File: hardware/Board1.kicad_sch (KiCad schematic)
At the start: 40 parts, among them IC1 AH1912-W-7, IC2 AH1912-W-7, J2 USB_C_Receptacle_USB2.0, J3 Conn_ST_STDC14, J4 Conn_01x02_Pin, J5 Conn_01x02_Pin, SW1 SW_Push, SW2 SW_Push, U1 STM32F042G6U6TR, U2 TS2940CW33_RPG, U3 STM32F072RBTx, U4 TJA1051T-3, Y1 8M

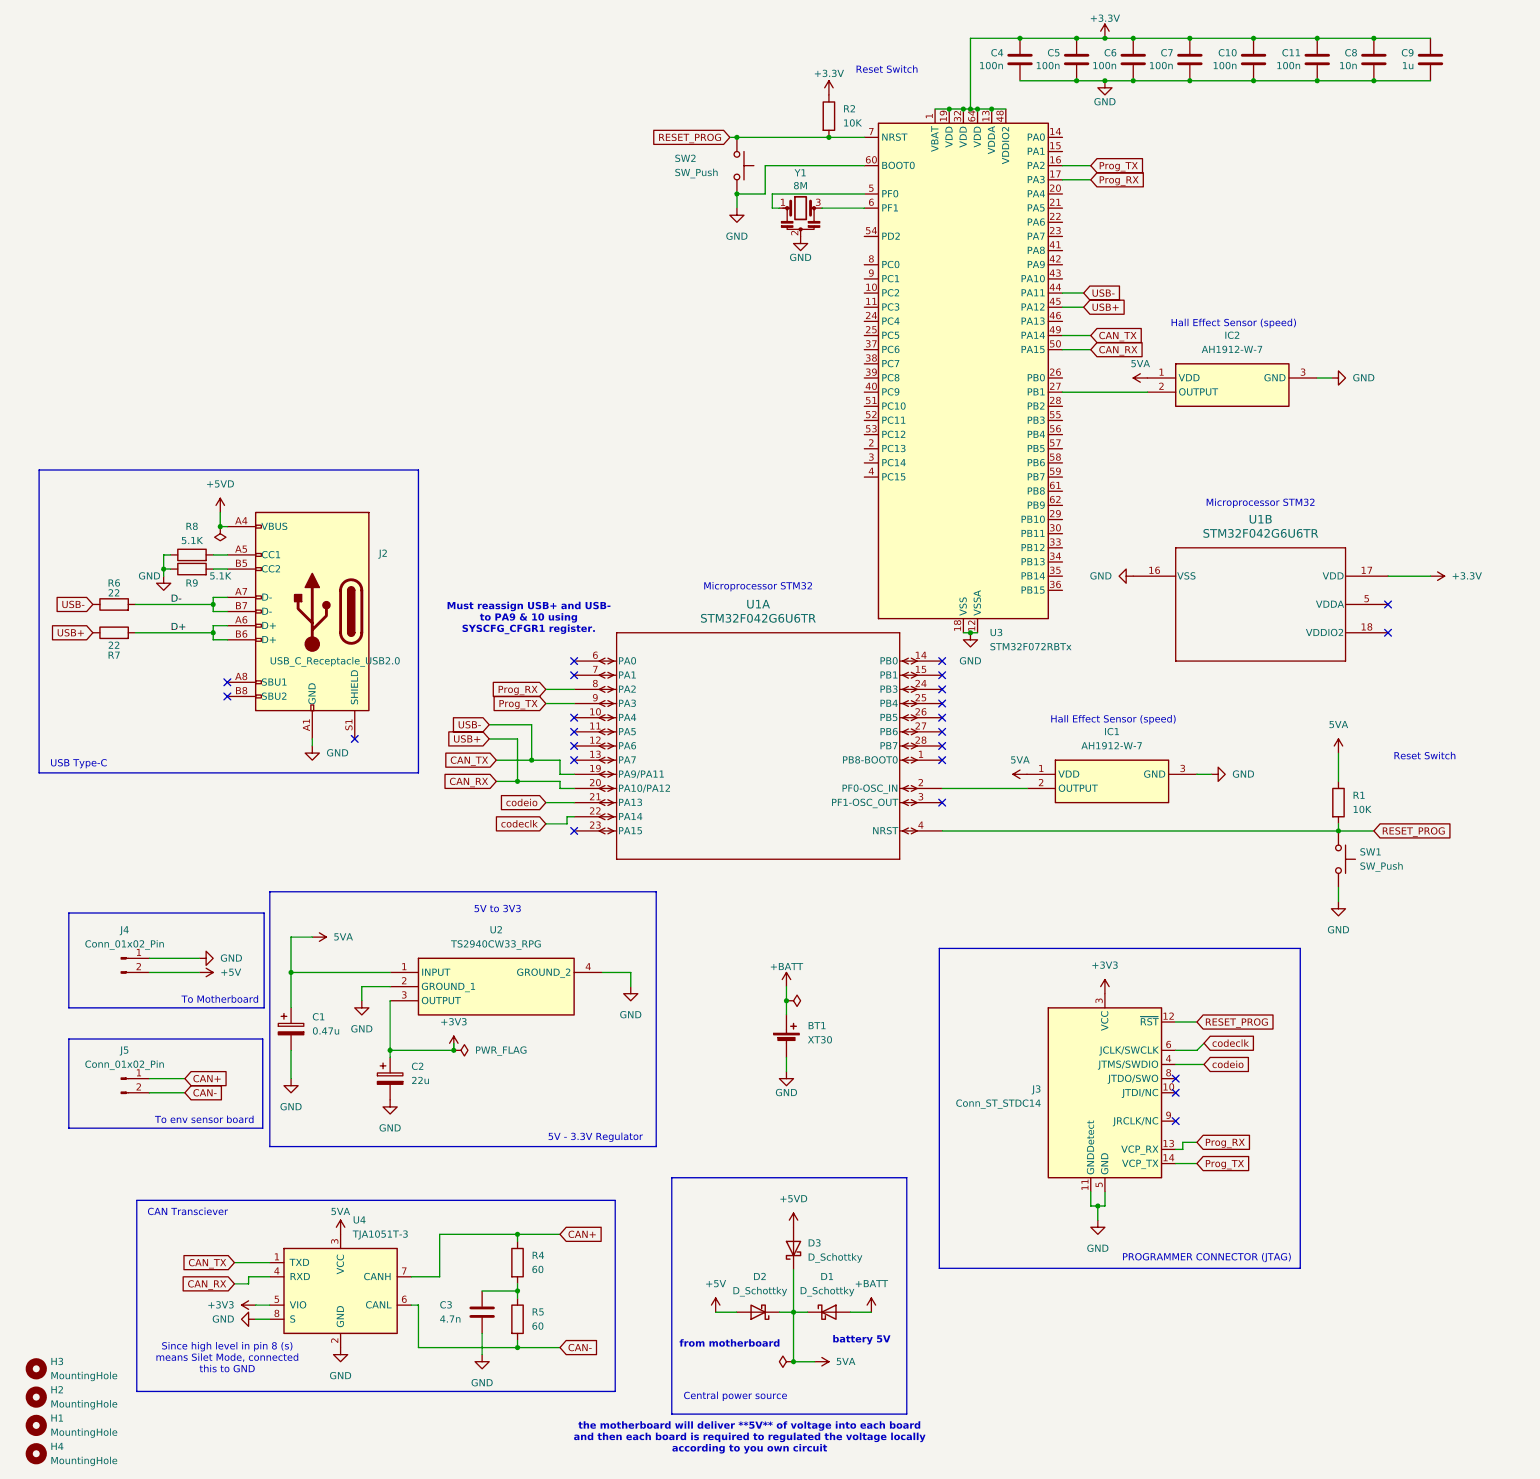
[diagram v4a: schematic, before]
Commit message: final revision of the speed and cadence board
Finished re routing the PCB and also did BOM and production needed for JLC PCB
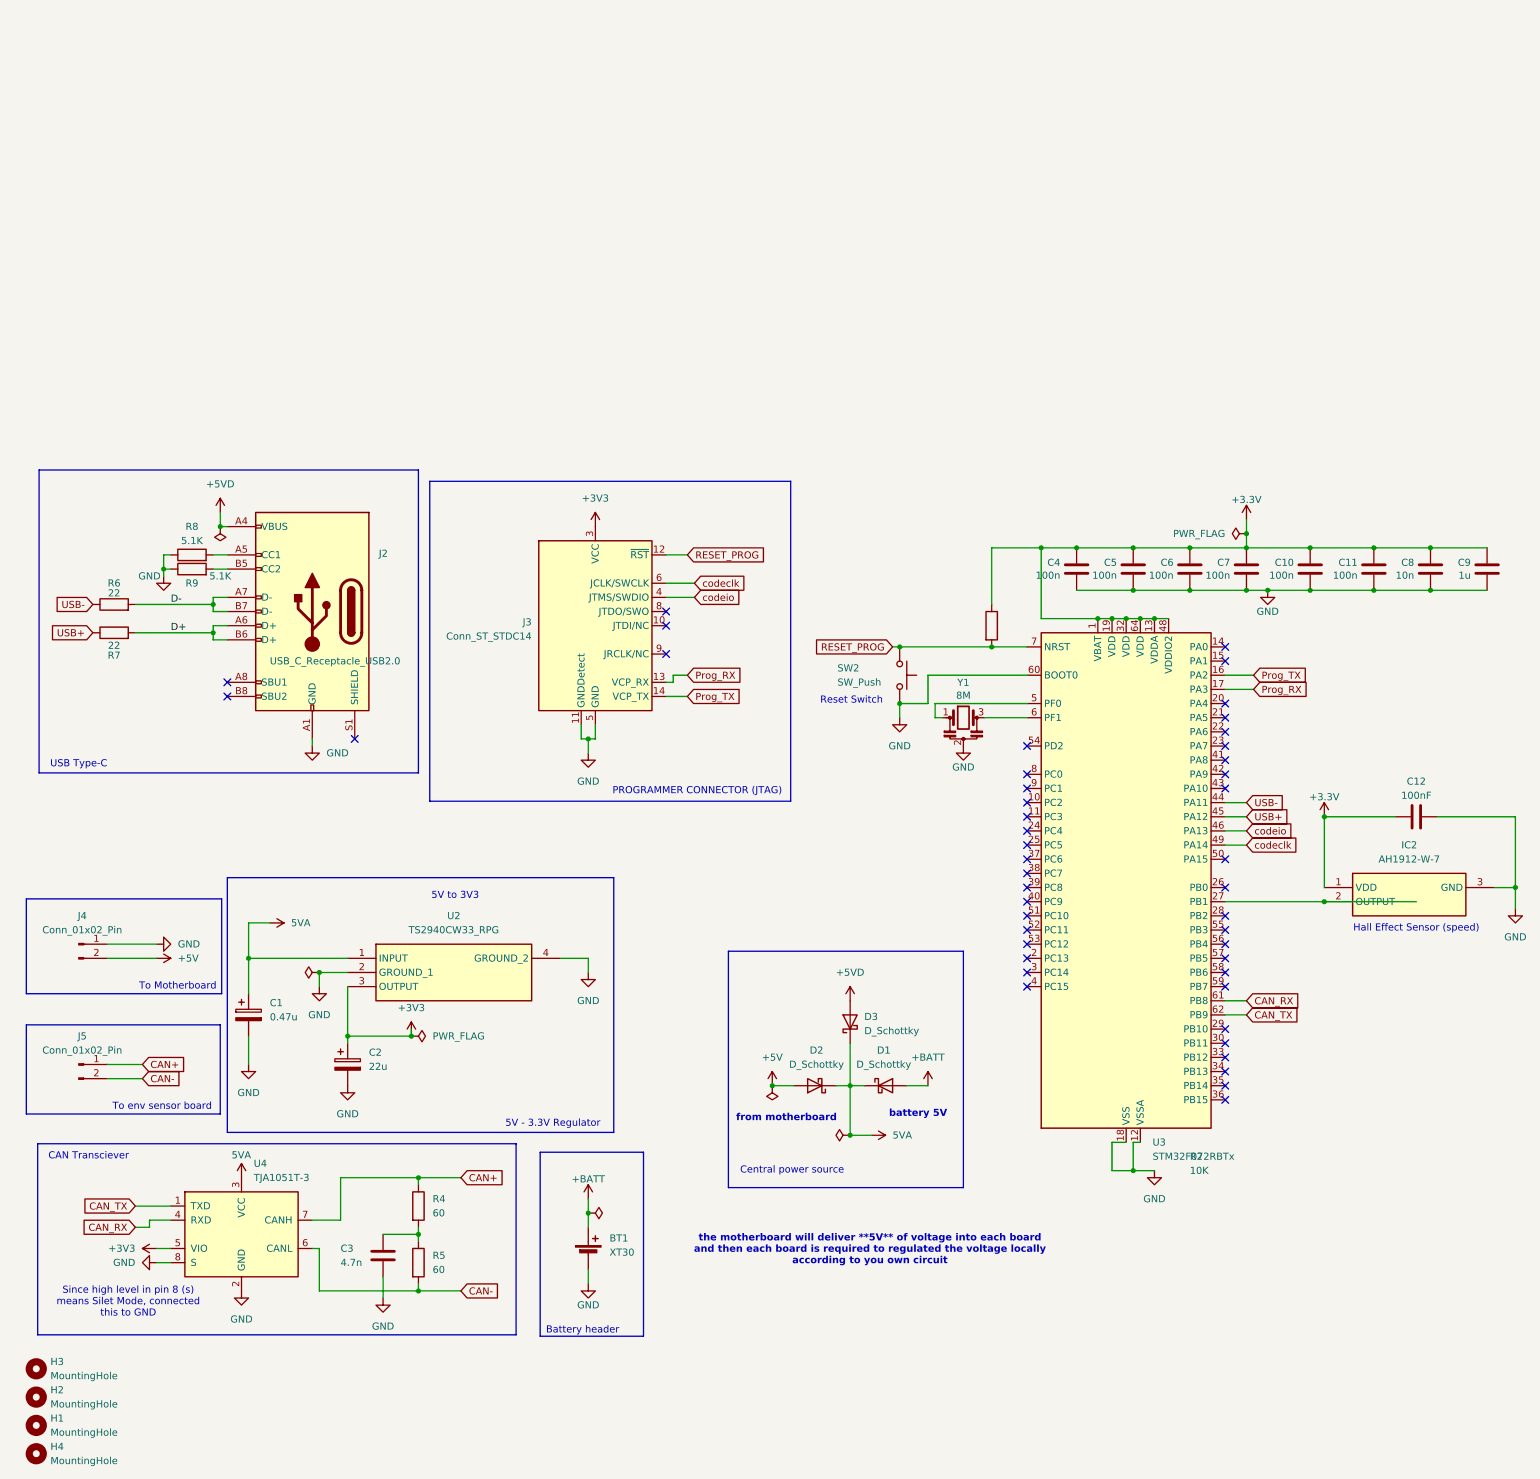
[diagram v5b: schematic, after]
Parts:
- removed IC1: AH1912-W-7, Package_TO_SOT_SMD:SC-59, symbol AH1912-W-7:AH1912-W-7
- removed R1: 10K, Resistor_SMD:R_0603_1608Metric, symbol Device:R
- removed SW1: SW_Push, Button_Switch_SMD:SW_SPST_SKQG_WithStem, symbol Switch:SW_Push
- removed U1: STM32F042G6U6TR, STM32:UFQFPN28-4x4mm-M, symbol STM32_:STM32F042G6U6TR
- added C12: 100nF, symbol Device:C
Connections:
- net +3.3V: now also IC2.1 (VDD), C12.1
- net 5VA: no longer IC2.1 (VDD)
- net CAN_RX: now also U3.61 (PB8); no longer R7.1, U3.45 (PA12), U3.50 (PA15)
- net CAN_TX: now also U3.62 (PB9); no longer R6.1, U3.44 (PA11), U3.49 (PA14)
- net GND: now also C12.2
- net codeclk: now also U3.49 (PA14)
- net codeio: now also U3.46 (PA13)
- new net USB+: R7.1, U3.45 (PA12)
- new net USB-: R6.1, U3.44 (PA11)
- no-connect marks 24 -> 46
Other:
- note added: "Battery header"
- note removed: "Microprocessor STM32"
- note removed: "Must reassign USB+ and USB- to PA9 & 10 using SYSCFG_CFGR1 register."
- moved on the sheet: BT1, C1, C10, C11, C2, C3, C4, C5, C6, C7, C8, C9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

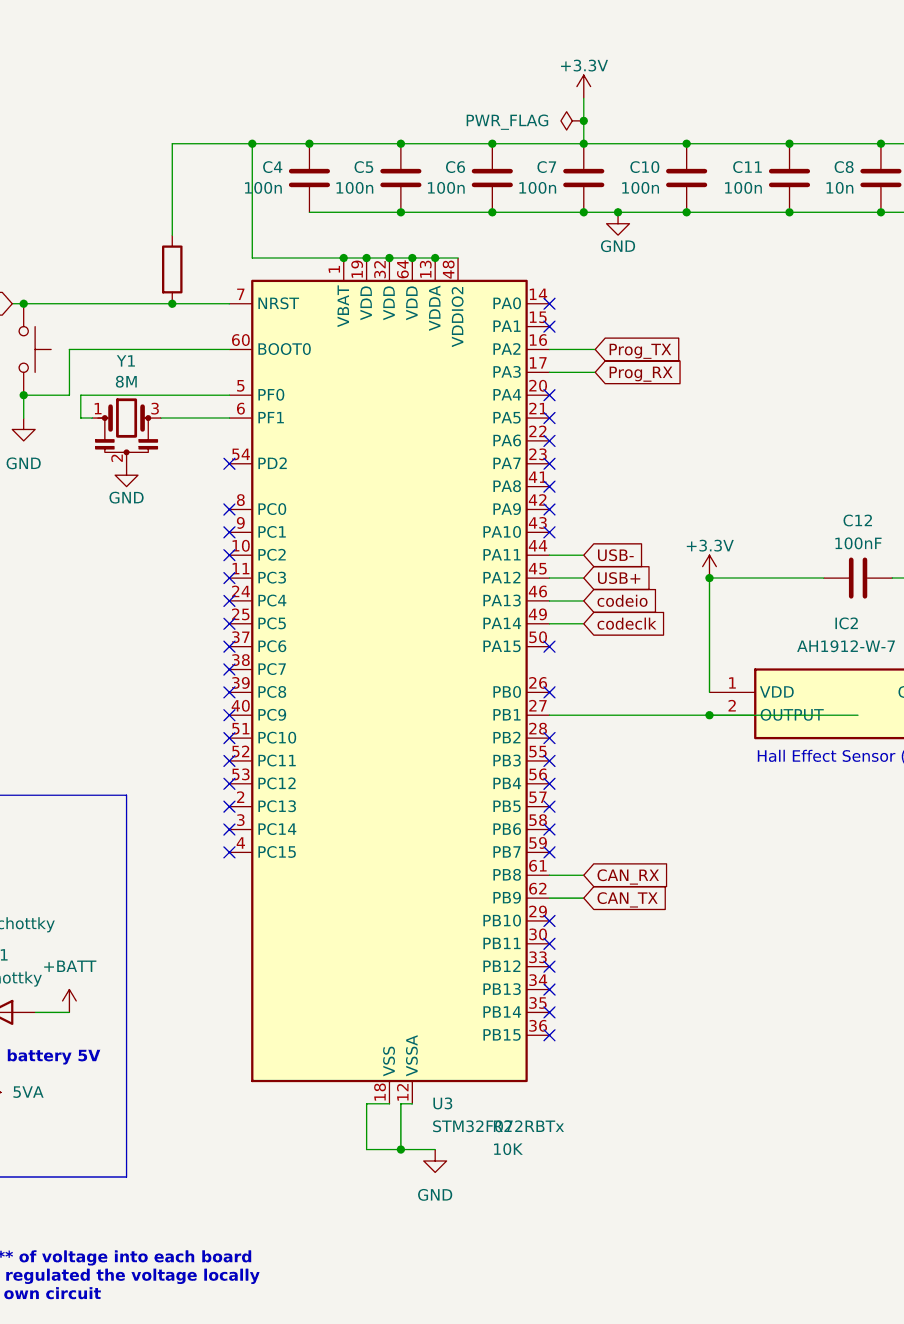
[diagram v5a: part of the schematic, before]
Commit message: Final small changes, only silkscreen stuff
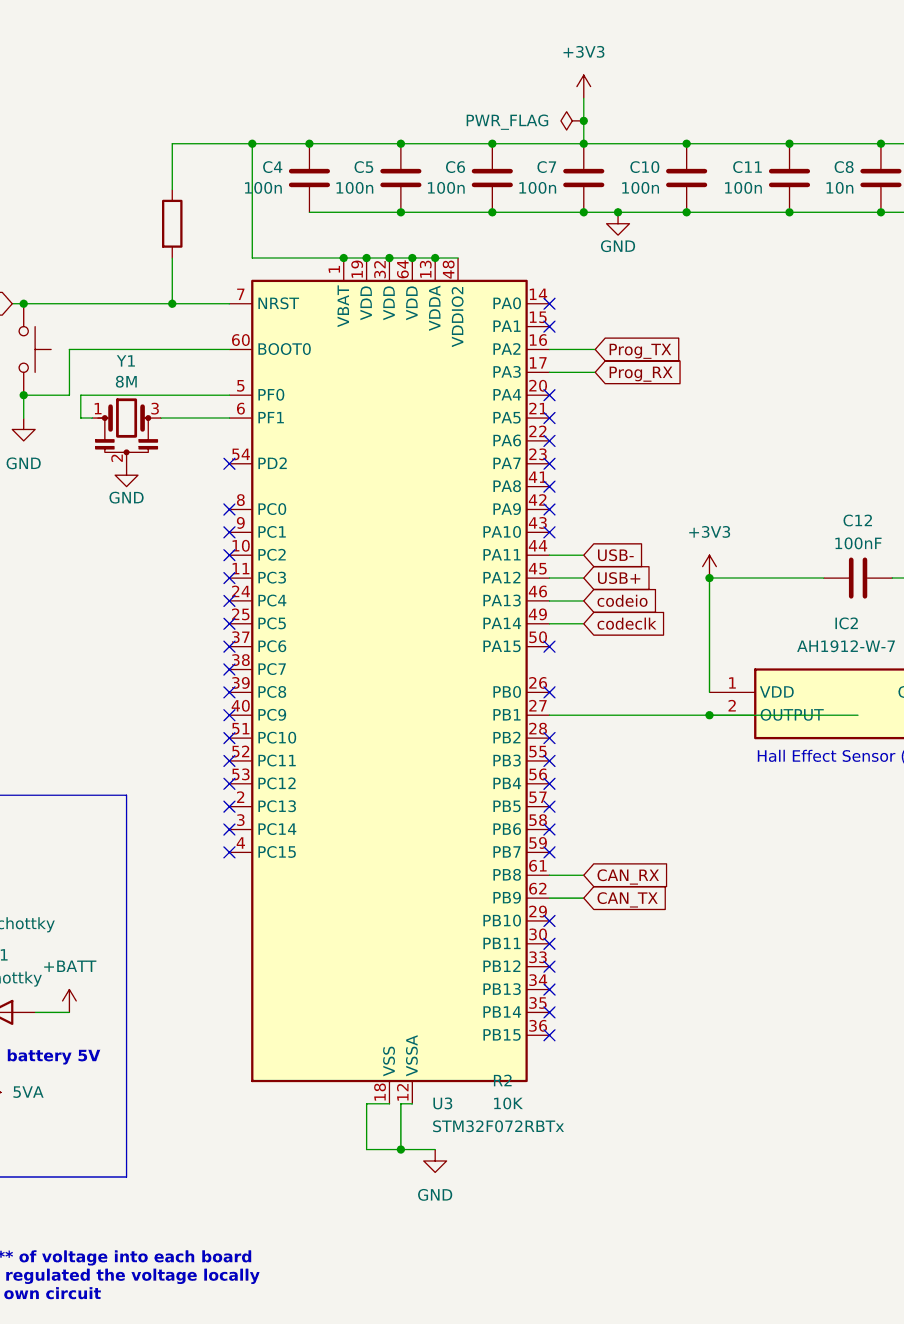
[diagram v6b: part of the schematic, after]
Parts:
- C12: footprint (none) -> Capacitor_SMD:C_0603_1608Metric
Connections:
- net +3.3V is gone; now on net +3V3: C10.2, C11.2, C12.1, C4.2, C5.2, C6.2, C7.2, C8.2, C9.2, IC2.1 (VDD), R2.1, U3.1 (VBAT), U3.13 (VDDA), U3.19 (VDD), U3.32 (VDD), U3.48 (VDDIO2), U3.64 (VDD)
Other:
- moved on the sheet: R2
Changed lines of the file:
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@@
 	)
 	(junction
-		(at 246.38 80.01)
-		(diameter 0)
-		(color 0 0 0 0)
-	)
-	(junction
 		(at 201.93 31.75)
 		(diameter 0)
@@
 	)
 	(junction
+		(at 246.38 80.01)
+		(diameter 0)
+		(color 0 0 0 0)
+	)
+	(junction
 		(at 205.74 44.45)
 		(diameter 0)
@@
 	(wire
 		(pts
-			(xy 186.69 31.75) (xy 186.69 41.91)
+			(xy 186.69 31.75) (xy 186.69 36.83)
 		)
 		(stroke
@@
 	(wire
 		(pts
+			(xy 186.69 44.45) (xy 186.69 49.53)
+		)
+		(stroke
+			(width 0)
+			(type default)
+		)
+	)
+	(wire
+		(pts
 			(xy 46.99 41.91) (xy 46.99 43.18)
 		)
@@
 	)
 	(symbol
+		(lib_id "power:+3V3")
+		(at 246.38 80.01 0)
+		(unit 1)
+		(exclude_from_sim no)
+		(in_bom yes)
+		(on_board yes)
+		(dnp no)
+		(fields_autoplaced yes)
+		(property "Reference" "#PWR02"
+			(at 246.38 83.82 0)
+			(effects
+				(font
+					(size 1.27 1.27)
+				)
+				(hide yes)
+			)
+		)
+		(property "Value" "+3V3"
+			(at 246.38 74.93 0)
+			(effects
+				(font
+					(size 1.27 1.27)
+				)
+			)
+		)
+		(property "Footprint" ""
+			(at 246.38 80.01 0)
+			(effects
+				(font
+					(size 1.27 1.27)
+				)
+				(hide yes)
+			)
+		)
+		(property "Datasheet" ""
+			(at 246.38 80.01 0)
+			(effects
+				(font
+					(size 1.27 1.27)
+				)
+				(hide yes)
+			)
+		)
+		(property "Description" "Power symbol creates a global label with name \"+3V3\""
+			(at 246.38 80.01 0)
+			(effects
+				(font
+					(size 1.27 1.27)
+				)
+				(hide yes)
+			)
+		)
+		(pin "1"
+		)
+		(instances
+			(project "Board1"
+				(path "/10163266-8018-4064-a980-f3c4e9dfe9d4"
+					(reference "#PWR02")
+					(unit 1)
+				)
+			)
+		)
+	)
+	(symbol
 		(lib_id "power:GND")
 		(at 170.18 62.23 0)
@@
 	(symbol
 		(lib_id "Device:R")
-		(at 186.69 45.72 0)
+		(at 186.69 40.64 0)
 		(unit 1)
 		(exclude_from_sim no)
@@
 		(dnp no)
 		(property "Reference" "R2"
-			(at 222.25 140.9699 0)
+			(at 222.25 135.8899 0)
 			(effects
 				(font
@@
 		)
 		(property "Value" "10K"
-			(at 222.25 143.5099 0)
+			(at 222.25 138.4299 0)
 			(effects
 				(font
@@
 		)
 		(property "Footprint" "Resistor_SMD:R_0603_1608Metric"
-			(at 184.912 45.72 90)
+			(at 184.912 40.64 90)
 			(effects
 				(font
@@
 		)
 		(property "Datasheet" "~"
-			(at 186.69 45.72 0)
+			(at 186.69 40.64 0)
 			(effects
 				(font
@@
 		)
 		(property "Description" "Resistor"
-			(at 186.69 45.72 0)
+			(at 186.69 40.64 0)
 			(effects
 				(font
@@
 	)
 	(symbol
+		(lib_id "power:+3V3")
+		(at 232.41 26.67 0)
+		(unit 1)
+		(exclude_from_sim no)
+		(in_bom yes)
+		(on_board yes)
+		(dnp no)
+		(fields_autoplaced yes)
+		(property "Reference" "#PWR01"
+			(at 232.41 30.48 0)
+			(effects
+				(font
+					(size 1.27 1.27)
+				)
+				(hide yes)
+			)
+		)
+		(property "Value" "+3V3"
+			(at 232.41 21.59 0)
+			(effects
+				(font
+					(size 1.27 1.27)
+				)
+			)
+		)
+		(property "Footprint" ""
+			(at 232.41 26.67 0)
+			(effects
+				(font
+					(size 1.27 1.27)
+				)
+				(hide yes)
+			)
+		)
+		(property "Datasheet" ""
+			(at 232.41 26.67 0)
+			(effects
+				(font
+					(size 1.27 1.27)
+				)
+				(hide yes)
+			)
+		)
+		(property "Description" "Power symbol creates a global label with name \"+3V3\""
+			(at 232.41 26.67 0)
+			(effects
+				(font
+					(size 1.27 1.27)
+				)
+				(hide yes)
+			)
+		)
+		(pin "1"
+		)
+		(instances
+			(project ""
+				(path "/10163266-8018-4064-a980-f3c4e9dfe9d4"
+					(reference "#PWR01")
+					(unit 1)
+				)
+			)
+		)
+	)
+	(symbol
 		(lib_id "Device:C")
 		(at 201.93 35.56 0)
@@
 	)
 	(symbol
-		(lib_id "power:+3.3V")
-		(at 246.38 80.01 0)
-		(unit 1)
-		(exclude_from_sim no)
-		(in_bom yes)
-		(on_board yes)
-		(dnp no)
-		(property "Reference" "#PWR039"
-			(at 246.38 83.82 0)
-			(effects
-				(font
-					(size 1.27 1.27)
-				)
-				(hide yes)
-			)
-		)
-		(property "Value" "+3.3V"
-			(at 246.38 76.454 0)
-			(effects
-				(font
-					(size 1.27 1.27)
-				)
-			)
-		)
-		(property "Footprint" ""
-			(at 246.38 80.01 0)
-			(effects
-				(font
-					(size 1.27 1.27)
-				)
-			)
-		)
-		(property "Datasheet" ""
-			(at 246.38 80.01 0)
-			(effects
-				(font
-					(size 1.27 1.27)
-				)
-			)
-		)
-		(property "Description" "Power symbol creates a global label with name \"+3.3V\""
-			(at 246.38 80.01 0)
-			(effects
-				(font
-					(size 1.27 1.27)
-				)
-				(hide yes)
-			)
-		)
-		(pin "1"
-		)
-		(instances
-			(project "Board1"
-				(path "/10163266-8018-4064-a980-f3c4e9dfe9d4"
-					(reference "#PWR039")
-					(unit 1)
-				)
-			)
-		)
-	)
-	(symbol
 		(lib_id "Device:D_Schottky")
 		(at 167.64 128.27 0)
@@
 	)
 	(symbol
-		(lib_id "power:+3.3V")
-		(at 232.41 26.67 0)
-		(unit 1)
-		(exclude_from_sim no)
-		(in_bom yes)
-		(on_board yes)
-		(dnp no)
-		(property "Reference" "#PWR016"
-			(at 232.41 30.48 0)
-			(effects
-				(font
-					(size 1.27 1.27)
-				)
-				(hide yes)
-			)
-		)
-		(property "Value" "+3.3V"
-			(at 232.41 23.114 0)
-			(effects
-				(font
-					(size 1.27 1.27)
-				)
-			)
-		)
-		(property "Footprint" ""
-			(at 232.41 26.67 0)
-			(effects
-				(font
-					(size 1.27 1.27)
-				)
-			)
-		)
-		(property "Datasheet" ""
-			(at 232.41 26.67 0)
-			(effects
-				(font
-					(size 1.27 1.27)
-				)
-			)
-		)
-		(property "Description" "Power symbol creates a global label with name \"+3.3V\""
-			(at 232.41 26.67 0)
-			(effects
-				(font
-					(size 1.27 1.27)
-				)
-				(hide yes)
-			)
-		)
-		(pin "1"
-		)
-		(instances
-			(project "Board1"
-				(path "/10163266-8018-4064-a980-f3c4e9dfe9d4"
-					(reference "#PWR016")
-					(unit 1)
-				)
-			)
-		)
-	)
-	(symbol
 		(lib_id "Device:C")
 		(at 265.43 35.56 0)
@@
 			)
 		)
-		(property "Footprint" ""
+		(property "Footprint" "Capacitor_SMD:C_0603_1608Metric"
 			(at 266.7 79.0448 0)
 			(effects
